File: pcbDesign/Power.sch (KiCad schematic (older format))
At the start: 41 parts

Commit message: Cerrected errors in the schematic and began work on the pcb layout
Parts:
- added C19, C20: 4.7u, Capacitor_SMD:C_0402_1005Metric, symbol Device:C
- D2, D3, D4, D5, D6: renamed from D?; footprint (none) -> Diode_SMD:D_0402_1005Metric
- U5: renamed from U?; footprint DSG0008A -> ul_LM2775QDSGTQ1:LM2775QDSGTQ1
- U6: renamed from U?; footprint SON_ULTRT_SEM -> ul_SC630AULTRT:SC630AULTRT
- gave numbers to parts that had none: 34
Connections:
- net GND: now also C19.1, C20.1
- net GPOUT_PIN: now also C19.2
- net VBUS_NREG: now also C20.2

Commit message: Fixed power rail enabling systems and rearanged pins for easier use
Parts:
- added R20, R21, R22: 10k, Resistor_SMD:R_0402_1005Metric, symbol Device:R_Small
- C17, C21: value C -> 2.2u
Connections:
- net CHARGE_ENABLE: now also R22.2
- net CHARGE_MODE_CH0: now also R20.2
- net CHARGE_MODE_CH1: now also R21.1
- net GND: now also R21.2, R22.1
- net GPOUT_PIN: now also R5.2
- net VBUS_NREG: no longer R5.2
- net at D2.1 (K), D3.1 (K), U7.13 (IN): now also R20.1
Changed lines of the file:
@@
 AR Path="/604D6BAE/604E1596" Ref="C17"  Part="1"
 F 0 "C17" H 4035 1354 50  0000 R CNN
-F 1 "C" H 4035 1445 50  0000 R CNN
+F 1 "2.2u" H 4035 1445 50  0000 R CNN
 F 2 "Capacitor_SMD:C_0402_1005Metric" H 4188 1250 50  0001 C CNN
 F 3 "~" H 4150 1400 50  0001 C CNN
@@
 AR Path="/604D6BAE/604E159C" Ref="C21"  Part="1"
 F 0 "C21" H 6585 1354 50  0000 R CNN
-F 1 "C" H 6585 1445 50  0000 R CNN
+F 1 "2.2u" H 6585 1445 50  0000 R CNN
 F 2 "Capacitor_SMD:C_0402_1005Metric" H 6738 1250 50  0001 C CNN
 F 3 "~" H 6700 1400 50  0001 C CNN
@@
 CHARGE_ENABLE
 Wire Wire Line
-	6900 3500 6900 3850
-Wire Wire Line
 	6900 3850 7100 3850
-Text GLabel 6500 4050 0    50   BiDi ~ 0
+Text GLabel 6150 4050 0    50   BiDi ~ 0
 CHARGE_MODE_CH0
-Wire Wire Line
-	7100 4050 6500 4050
-Text GLabel 6500 4150 0    50   BiDi ~ 0
+Text GLabel 6150 4150 0    50   BiDi ~ 0
 CHARGE_MODE_CH1
-Wire Wire Line
-	6500 4150 7100 4150
 $Comp
 L power:GND #PWR?
@@
 	2750 3400 2550 3400
 Wire Wire Line
-	2350 3400 2350 3300
-Wire Wire Line
 	2350 3200 2600 3200
 $Comp
@@
 	1    0    0    -1
 $EndComp
-$Comp
-L Device:R_Small R?
-U 1 1 605F8711
-P 2250 3400
-AR Path="/605F8711" Ref="R?"  Part="1"
-AR Path="/604D6BAE/605F8711" Ref="R5"  Part="1"
-F 0 "R5" H 2309 3446 50  0000 L CNN
-F 1 "10k" H 2309 3355 50  0000 L CNN
-F 2 "Resistor_SMD:R_0402_1005Metric" H 2250 3400 50  0001 C CNN
-F 3 "~" H 2250 3400 50  0001 C CNN
-	1    2250 3400
-	-1   0    0    1
-$EndComp
-Wire Wire Line
-	2100 3500 2250 3500
 Connection ~ 2750 3500
-Connection ~ 2250 3500
-Wire Wire Line
-	2250 3500 2750 3500
-Wire Wire Line
-	2250 3300 2350 3300
-Connection ~ 2350 3300
-Wire Wire Line
-	2350 3300 2350 3200
 Text GLabel 1500 2500 0    50   BiDi ~ 0
 EN
@@
 	-1   0    0    1
 $EndComp
+Wire Wire Line
+	2100 3500 2350 3500
+Wire Wire Line
+	2350 3200 2350 3400
+$Comp
+L Device:R_Small R?
+U 1 1 60446814
+P 2350 3600
+AR Path="/60446814" Ref="R?"  Part="1"
+AR Path="/604D6BAE/60446814" Ref="R5"  Part="1"
+F 0 "R5" H 2409 3646 50  0000 L CNN
+F 1 "10k" H 2409 3555 50  0000 L CNN
+F 2 "Resistor_SMD:R_0402_1005Metric" H 2350 3600 50  0001 C CNN
+F 3 "~" H 2350 3600 50  0001 C CNN
+	1    2350 3600
+	-1   0    0    -1
+$EndComp
+Connection ~ 2350 3500
+Wire Wire Line
+	2350 3500 2750 3500
+Text GLabel 2150 3700 0    50   BiDi ~ 0
+VBUS_3V3_CH0_REG
+Wire Wire Line
+	2150 3700 2350 3700
+$Comp
+L Device:R_Small R?
+U 1 1 6044EFF2
+P 6900 3300
+AR Path="/6044EFF2" Ref="R?"  Part="1"
+AR Path="/604D6BAE/6044EFF2" Ref="R22"  Part="1"
+F 0 "R22" H 6959 3346 50  0000 L CNN
+F 1 "10k" H 6959 3255 50  0000 L CNN
+F 2 "Resistor_SMD:R_0402_1005Metric" H 6900 3300 50  0001 C CNN
+F 3 "~" H 6900 3300 50  0001 C CNN
+	1    6900 3300
+	-1   0    0    -1
+$EndComp
+Wire Wire Line
+	6900 3400 6900 3850
+$Comp
+L power:GND #PWR?
+U 1 1 60453D31
+P 6900 3200
+AR Path="/60453D31" Ref="#PWR?"  Part="1"
+AR Path="/604D6BAE/60453D31" Ref="#PWR0114"  Part="1"
+F 0 "#PWR0114" H 6900 2950 50  0001 C CNN
+F 1 "GND" H 6905 3027 50  0000 C CNN
+F 2 "" H 6900 3200 50  0001 C CNN
+F 3 "" H 6900 3200 50  0001 C CNN
+	1    6900 3200
+	-1   0    0    1
+$EndComp
+$Comp
+L Device:R_Small R?
+U 1 1 604579F6
+P 6300 4250
+AR Path="/604579F6" Ref="R?"  Part="1"
+AR Path="/604D6BAE/604579F6" Ref="R21"  Part="1"
+F 0 "R21" H 6359 4296 50  0000 L CNN
+F 1 "10k" H 6359 4205 50  0000 L CNN
+F 2 "Resistor_SMD:R_0402_1005Metric" H 6300 4250 50  0001 C CNN
+F 3 "~" H 6300 4250 50  0001 C CNN
+	1    6300 4250
+	-1   0    0    -1
+$EndComp
+$Comp
+L Device:R_Small R?
+U 1 1 6045A6CE
+P 6300 3950
+AR Path="/6045A6CE" Ref="R?"  Part="1"
+AR Path="/604D6BAE/6045A6CE" Ref="R20"  Part="1"
+F 0 "R20" H 6359 3996 50  0000 L CNN
+F 1 "10k" H 6359 3905 50  0000 L CNN
+F 2 "Resistor_SMD:R_0402_1005Metric" H 6300 3950 50  0001 C CNN
+F 3 "~" H 6300 3950 50  0001 C CNN
+	1    6300 3950
+	-1   0    0    -1
+$EndComp
+Wire Wire Line
+	6150 4050 6300 4050
+Connection ~ 6300 4050
+Wire Wire Line
+	6300 4050 7100 4050
+Wire Wire Line
+	6150 4150 6300 4150
+Connection ~ 6300 4150
+Wire Wire Line
+	6300 4150 7100 4150
+Wire Wire Line
+	7600 3450 7050 3450
+Wire Wire Line
+	7050 3450 7050 2900
+Wire Wire Line
+	7050 2900 6150 2900
+Wire Wire Line
+	6150 2900 6150 3600
+Wire Wire Line
+	6150 3600 6300 3600
+Wire Wire Line
+	6300 3600 6300 3850
+$Comp
+L power:GND #PWR?
+U 1 1 60476435
+P 6300 4350
+AR Path="/60476435" Ref="#PWR?"  Part="1"
+AR Path="/604D6BAE/60476435" Ref="#PWR0115"  Part="1"
+F 0 "#PWR0115" H 6300 4100 50  0001 C CNN
+F 1 "GND" H 6305 4177 50  0000 C CNN
+F 2 "" H 6300 4350 50  0001 C CNN
+F 3 "" H 6300 4350 50  0001 C CNN
+	1    6300 4350
+	1    0    0    -1
+$EndComp
 $EndSCHEMATC

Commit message: Finnished routing
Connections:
- net VBUS_BAT_NREG: now also C22.1, U7.10 (OUT), U7.11 (OUT)
- net GPOUT_PIN renamed VBUS_3V3_CH0_REG
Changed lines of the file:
@@
 Wire Wire Line
 	10650 3300 10650 4000
-Text GLabel 10550 4000 3    50   BiDi ~ 0
-GPOUT_PIN
 Connection ~ 7600 3450
 Wire Wire Line
@@
 	1    0    0    -1
 $EndComp
+Text GLabel 8100 3250 1    50   BiDi ~ 0
+VBUS_BAT_NREG
 $EndSCHEMATC

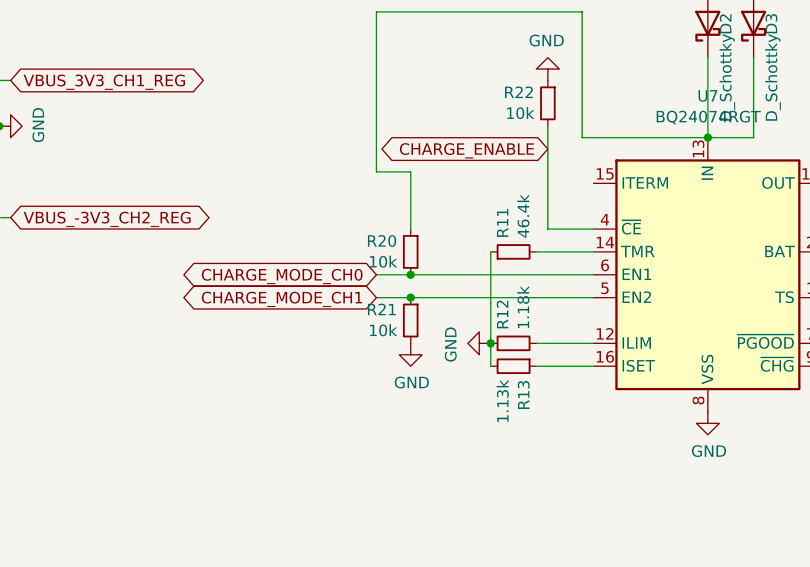
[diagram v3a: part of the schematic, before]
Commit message: Reconfigured charging circuit
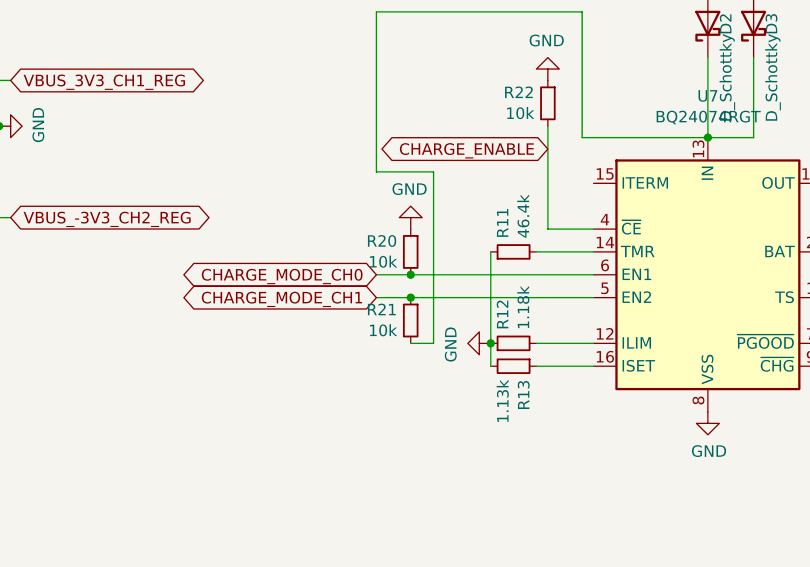
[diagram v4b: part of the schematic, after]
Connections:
- net GND: now also R20.1; no longer R21.2
- net at D2.1 (K), D3.1 (K), U7.13 (IN): now also R21.2; no longer R20.1
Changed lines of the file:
@@
 Wire Wire Line
 	6150 2900 6150 3600
-Wire Wire Line
-	6150 3600 6300 3600
-Wire Wire Line
-	6300 3600 6300 3850
 $Comp
 L power:GND #PWR?
 U 1 1 60476435
-P 6300 4350
+P 6300 3850
 AR Path="/60476435" Ref="#PWR?"  Part="1"
 AR Path="/604D6BAE/60476435" Ref="#PWR0115"  Part="1"
-F 0 "#PWR0115" H 6300 4100 50  0001 C CNN
-F 1 "GND" H 6305 4177 50  0000 C CNN
-F 2 "" H 6300 4350 50  0001 C CNN
-F 3 "" H 6300 4350 50  0001 C CNN
-	1    6300 4350
-	1    0    0    -1
+F 0 "#PWR0115" H 6300 3600 50  0001 C CNN
+F 1 "GND" H 6305 3677 50  0000 C CNN
+F 2 "" H 6300 3850 50  0001 C CNN
+F 3 "" H 6300 3850 50  0001 C CNN
+	1    6300 3850
+	-1   0    0    1
 $EndComp
 Text GLabel 8100 3250 1    50   BiDi ~ 0
 VBUS_BAT_NREG
+Wire Wire Line
+	6400 3600 6400 4350
+Wire Wire Line
+	6400 4350 6300 4350
+Wire Wire Line
+	6150 3600 6400 3600
 $EndSCHEMATC

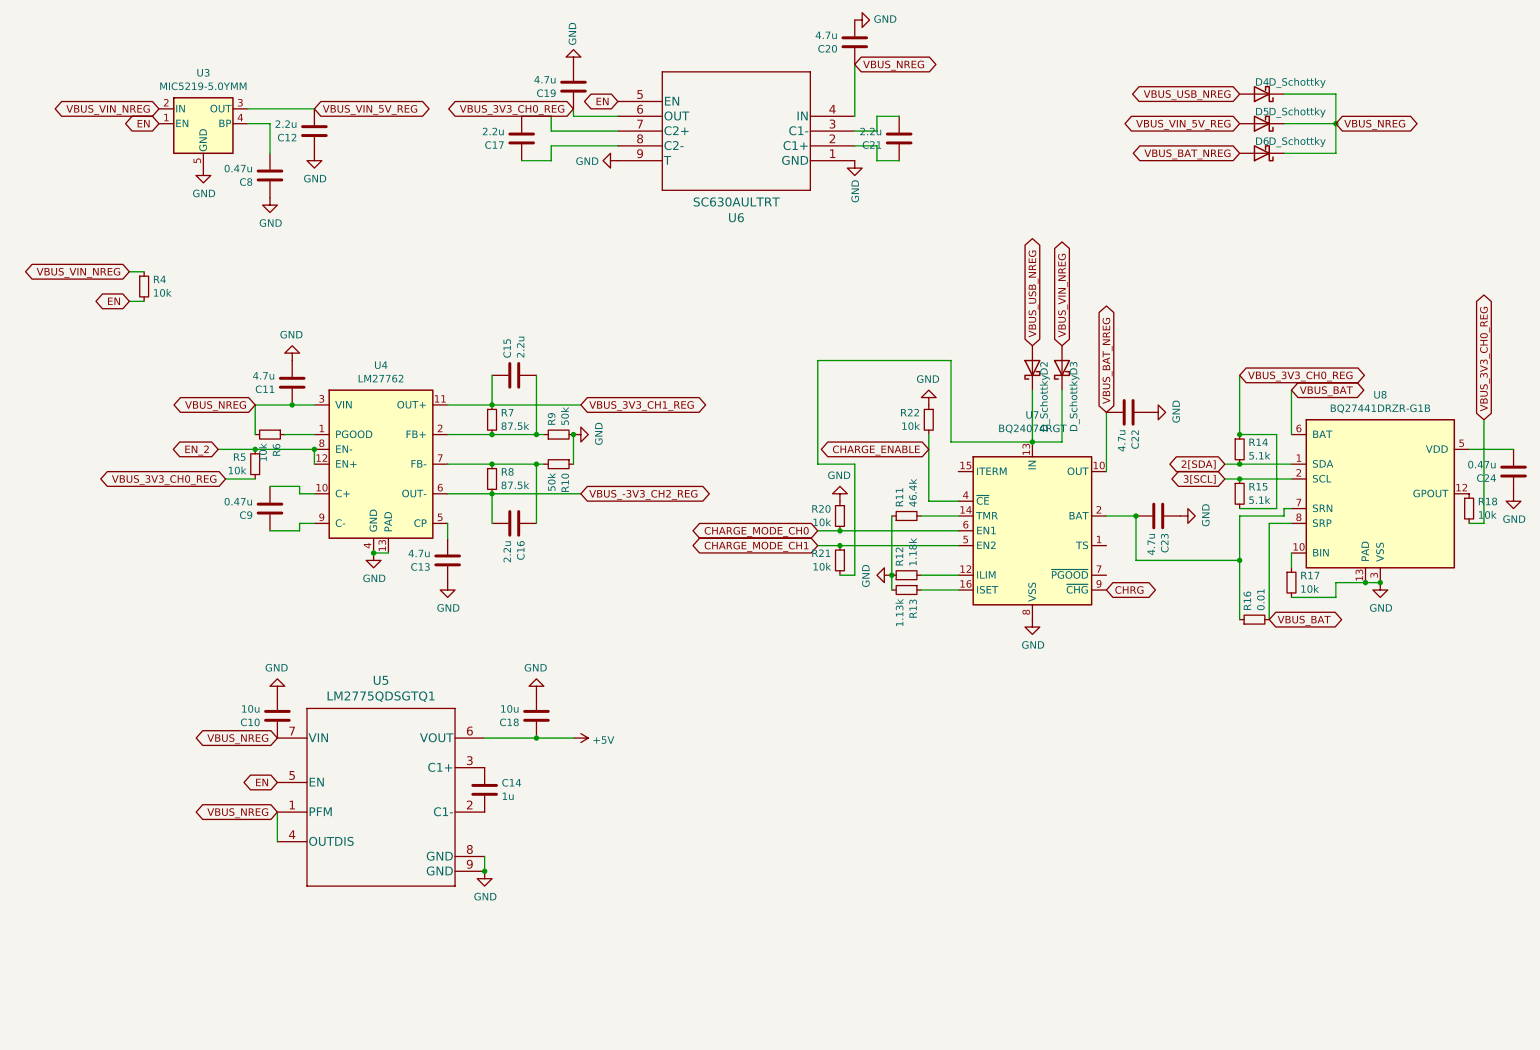
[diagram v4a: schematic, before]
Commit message: Swapped components for more avaiable ones
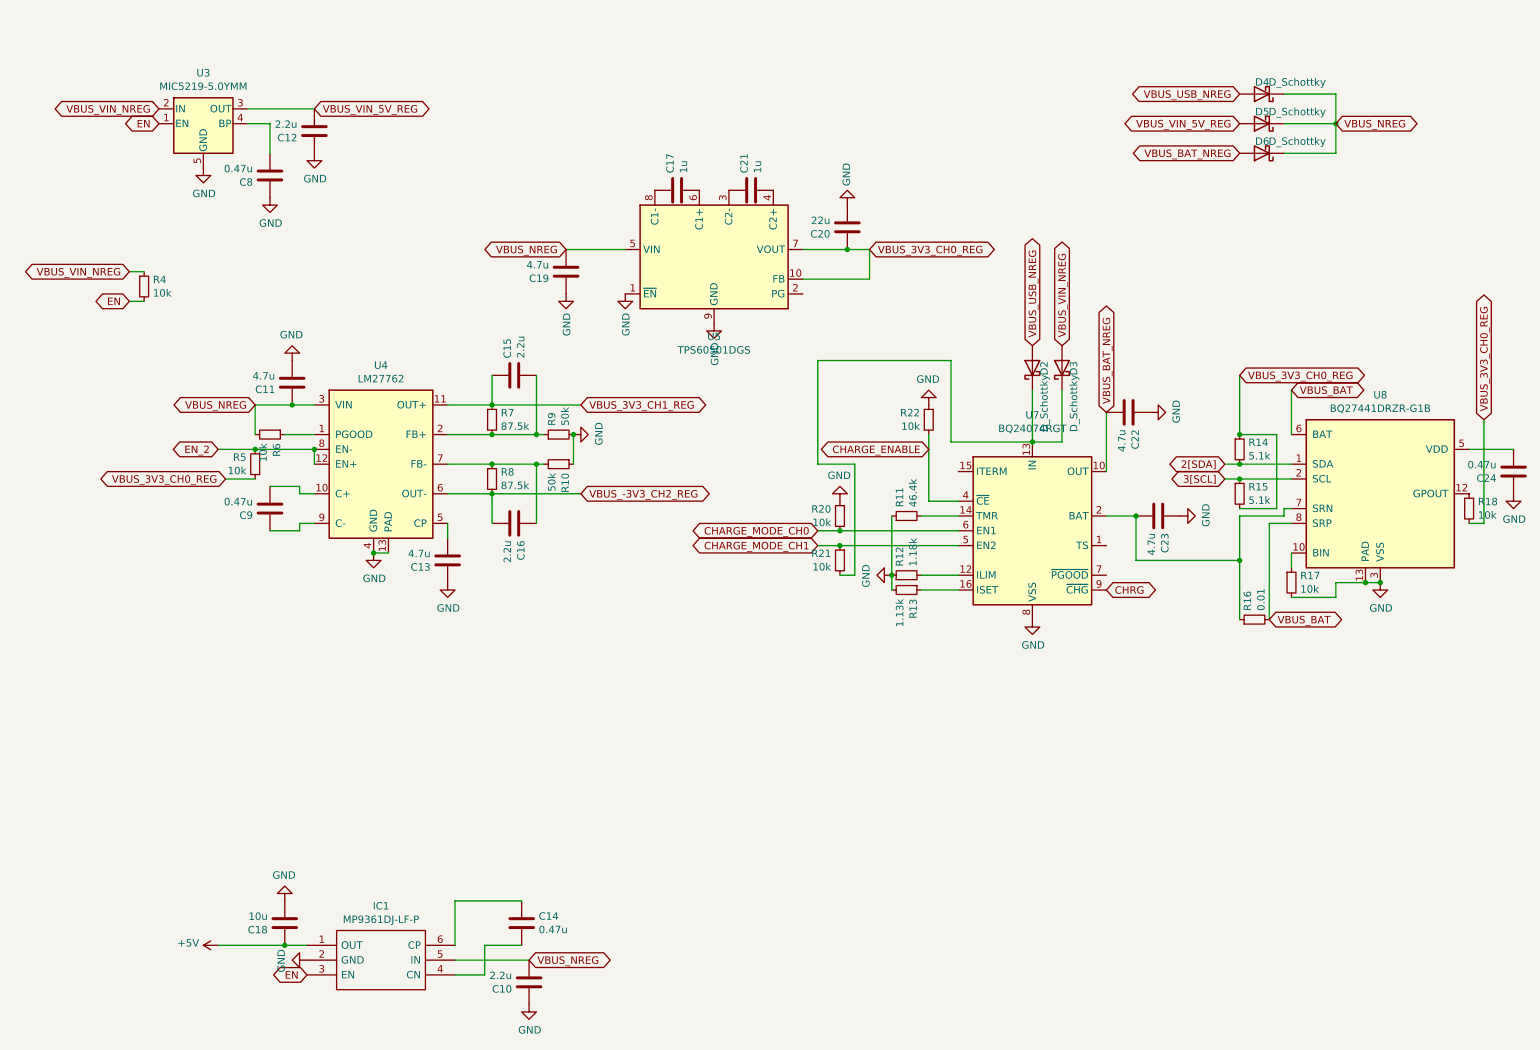
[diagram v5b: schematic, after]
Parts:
- removed U5: LM2775QDSGTQ1, ul_LM2775QDSGTQ1:LM2775QDSGTQ1, symbol ATSAME51J18A-devboard-rescue:LM2775QDSGTQ1-2021-03-01_13-50-06
- removed U6: SC630AULTRT, ul_SC630AULTRT:SC630AULTRT, symbol ATSAME51J18A-devboard-rescue:SC630AULTRT-2021-03-02_13-26-31
- added IC1: MP9361DJ-LF-P, SamacSys_Parts:SOT95P280X100-6N, symbol SamacSys_Parts:MP9361DJ-LF-P
- added U5: TPS60501DGS, Package_SO:MSOP-10_3x3mm_P0.5mm, symbol Regulator_SwitchedCapacitor:TPS60501DGS
- C10: value 10u -> 2.2u
- C14: value 1u -> 0.47u
- C17, C21: value 2.2u -> 1u
- C20: value 4.7u -> 22u
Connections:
- net +5V: now also IC1.1 (OUT)
- net EN: now also IC1.3 (EN)
- net GND: now also C10.2, C19.2, IC1.2 (GND), U5.1 (~EN), U5.9 (GND); no longer C10.1, C19.1
- net VBUS_3V3_CH0_REG: now also C20.2, U5.10 (FB), U5.7 (VOUT); no longer C19.2
- net VBUS_NREG: now also C10.1, C19.1, IC1.5 (IN), U5.5 (VIN); no longer C10.2, C20.2
- net at C21.2: now also U5.3 (C2-)
- net at C21.1: now also U5.4 (C2+)
- net at C17.1: now also U5.6 (C1+)
- net at C17.2: now also U5.8 (C1-)
- net at C14.1: now also IC1.4 (CN)
- net at C14.2: now also IC1.6 (CP)
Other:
- moved on the sheet: C10, C14, C17, C18, C19, C20, C21

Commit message: Begun to make changes to the design
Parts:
- removed C11, C13: 4.7u, Capacitor_SMD:C_0402_1005Metric, symbol Device:C
- removed C15, C16: 2.2u, Capacitor_SMD:C_0402_1005Metric, symbol Device:C
- removed C17, C21: 1u, Capacitor_SMD:C_0402_1005Metric, symbol Device:C
- removed C9: 0.47u, Capacitor_SMD:C_0402_1005Metric, symbol Device:C
- removed R10, R9: 50k, Resistor_SMD:R_0402_1005Metric, symbol Device:R_Small
- removed R5, R6: 10k, Resistor_SMD:R_0402_1005Metric, symbol Device:R_Small
- removed R7, R8: 87.5k, Resistor_SMD:R_0402_1005Metric, symbol Device:R_Small
- removed U4: LM27762, Package_SON:WSON-12-1EP_3x2mm_P0.5mm_EP1x2.65_ThermalVias, symbol Regulator_SwitchedCapacitor:LM27762
- removed U5: TPS60501DGS, Package_SO:MSOP-10_3x3mm_P0.5mm, symbol Regulator_SwitchedCapacitor:TPS60501DGS
- added U?: AP2204K-3.3, Package_TO_SOT_SMD:SOT-23-5, symbol Regulator_Linear:AP2204K-3.3
- IC1: symbol SamacSys_Parts:MP9361DJ-LF-P -> ATSAME51J18A-devboard-rescue:MP9361DJ-LF-P-SamacSys_Parts
